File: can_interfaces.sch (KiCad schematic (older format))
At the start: 14 parts

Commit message: interface panel connector
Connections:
- net CAN1L: now reaches CONN?.4 (CANL), CONN?.4 (CANL), CONN?.4 (CANL), CONN?.4 (CANL), CONN?.4 (CANL), CONN?.4 (CANL), CONN?.4 (CANL), U?.6 (CANL)
- net CAN1H: now reaches CONN?.3 (CANH), CONN?.3 (CANH), CONN?.3 (CANH), CONN?.3 (CANH), CONN?.3 (CANH), CONN?.3 (CANH), CONN?.3 (CANH), U?.7 (CANH)
- net CAN2L: now reaches CONN?.4 (CANL), CONN?.4 (CANL), CONN?.4 (CANL), U?.6 (CANL)
- net CAN2H: now reaches CONN?.3 (CANH), CONN?.3 (CANH), CONN?.3 (CANH), U?.7 (CANH)
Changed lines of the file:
@@
 	1    0    0    -1
 $EndComp
+Text HLabel 4100 1000 0    60   BiDi ~ 0
+CAN1H
+Text HLabel 4100 1100 0    60   BiDi ~ 0
+CAN1L
+Text HLabel 9300 1000 0    60   BiDi ~ 0
+CAN2H
+Text HLabel 9300 1100 0    60   BiDi ~ 0
+CAN2L
 Wire Wire Line
 	2250 2100 2250 2150
@@
 	4300 6500 4400 6500
 Wire Wire Line
-	4300 1700 4300 6500
+	4300 1000 4300 6500
 Connection ~ 4300 1700
 Wire Wire Line
 	4200 6600 4400 6600
 Wire Wire Line
-	4200 1800 4200 6600
+	4200 1100 4200 6600
 Connection ~ 4200 1800
 Wire Wire Line
@@
 Connection ~ 4300 5700
 Wire Wire Line
-	9600 3300 9500 3300
+	9500 3300 9600 3300
 Wire Wire Line
-	9600 3400 9400 3400
+	9400 3400 9600 3400
 Wire Wire Line
 	9600 2600 9400 2600
@@
 Connection ~ 9500 2500
 Wire Wire Line
-	9600 1700 8900 1700
+	8900 1700 9600 1700
 Wire Wire Line
 	8900 1800 9600 1800
 Wire Wire Line
-	9400 3400 9400 1800
+	9400 1100 9400 3400
 Connection ~ 9400 1800
 Wire Wire Line
-	9500 3300 9500 1700
+	9500 1000 9500 3300
 Connection ~ 9500 1700
+Wire Wire Line
+	4100 1100 4200 1100
+Wire Wire Line
+	4300 1000 4100 1000
+Wire Wire Line
+	9300 1100 9400 1100
+Wire Wire Line
+	9300 1000 9500 1000
 $EndSCHEMATC

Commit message: gpio assignment, servos PWM chip
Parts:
- removed CONN?: CAN, MODULE, symbol CAN
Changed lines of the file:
@@
 $Descr A4 11693 8268
 encoding utf-8
-Sheet 2 2
+Sheet 2 3
 Title ""
 Date ""
@@
 	1    0    0    -1
 $EndComp
-$Comp
-L CAN CONN?
-U 1 1 5817684A
-P 9950 3250
-F 0 "CONN?" H 9950 3600 50  0000 C CNN
-F 1 "CAN" H 9950 2900 50  0000 C CNN
-F 2 "MODULE" H 10200 3250 50  0001 C CNN
-F 3 "DOCUMENTATION" H 10200 3250 50  0001 C CNN
-	1    9950 3250
-	1    0    0    -1
-$EndComp
-$Comp
-L GND #PWR?
-U 1 1 58176850
-P 9600 3200
-F 0 "#PWR?" H 9600 3200 30  0001 C CNN
-F 1 "GND" H 9600 3130 30  0001 C CNN
-F 2 "" H 9600 3200 60  0000 C CNN
-F 3 "" H 9600 3200 60  0000 C CNN
-	1    9600 3200
-	1    0    0    -1
-$EndComp
-$Comp
-L +5V #PWR?
-U 1 1 58176856
-P 9600 3100
-F 0 "#PWR?" H 9600 3190 20  0001 C CNN
-F 1 "+5V" H 9600 3190 30  0000 C CNN
-F 2 "" H 9600 3100 60  0000 C CNN
-F 3 "" H 9600 3100 60  0000 C CNN
-	1    9600 3100
-	1    0    0    -1
-$EndComp
 Text HLabel 4100 1000 0    60   BiDi ~ 0
 CAN1H
@@
 Connection ~ 4300 5700
 Wire Wire Line
-	9500 3300 9600 3300
-Wire Wire Line
-	9400 3400 9600 3400
-Wire Wire Line
-	9600 2600 9400 2600
-Connection ~ 9400 2600
-Wire Wire Line
-	9600 2500 9500 2500
-Connection ~ 9500 2500
+	9400 2600 9600 2600
+Wire Wire Line
+	9500 2500 9600 2500
 Wire Wire Line
 	8900 1700 9600 1700
@@
 	8900 1800 9600 1800
 Wire Wire Line
-	9400 1100 9400 3400
+	9400 1100 9400 2600
 Connection ~ 9400 1800
 Wire Wire Line
-	9500 1000 9500 3300
+	9500 1000 9500 2500
 Connection ~ 9500 1700
 Wire Wire Line

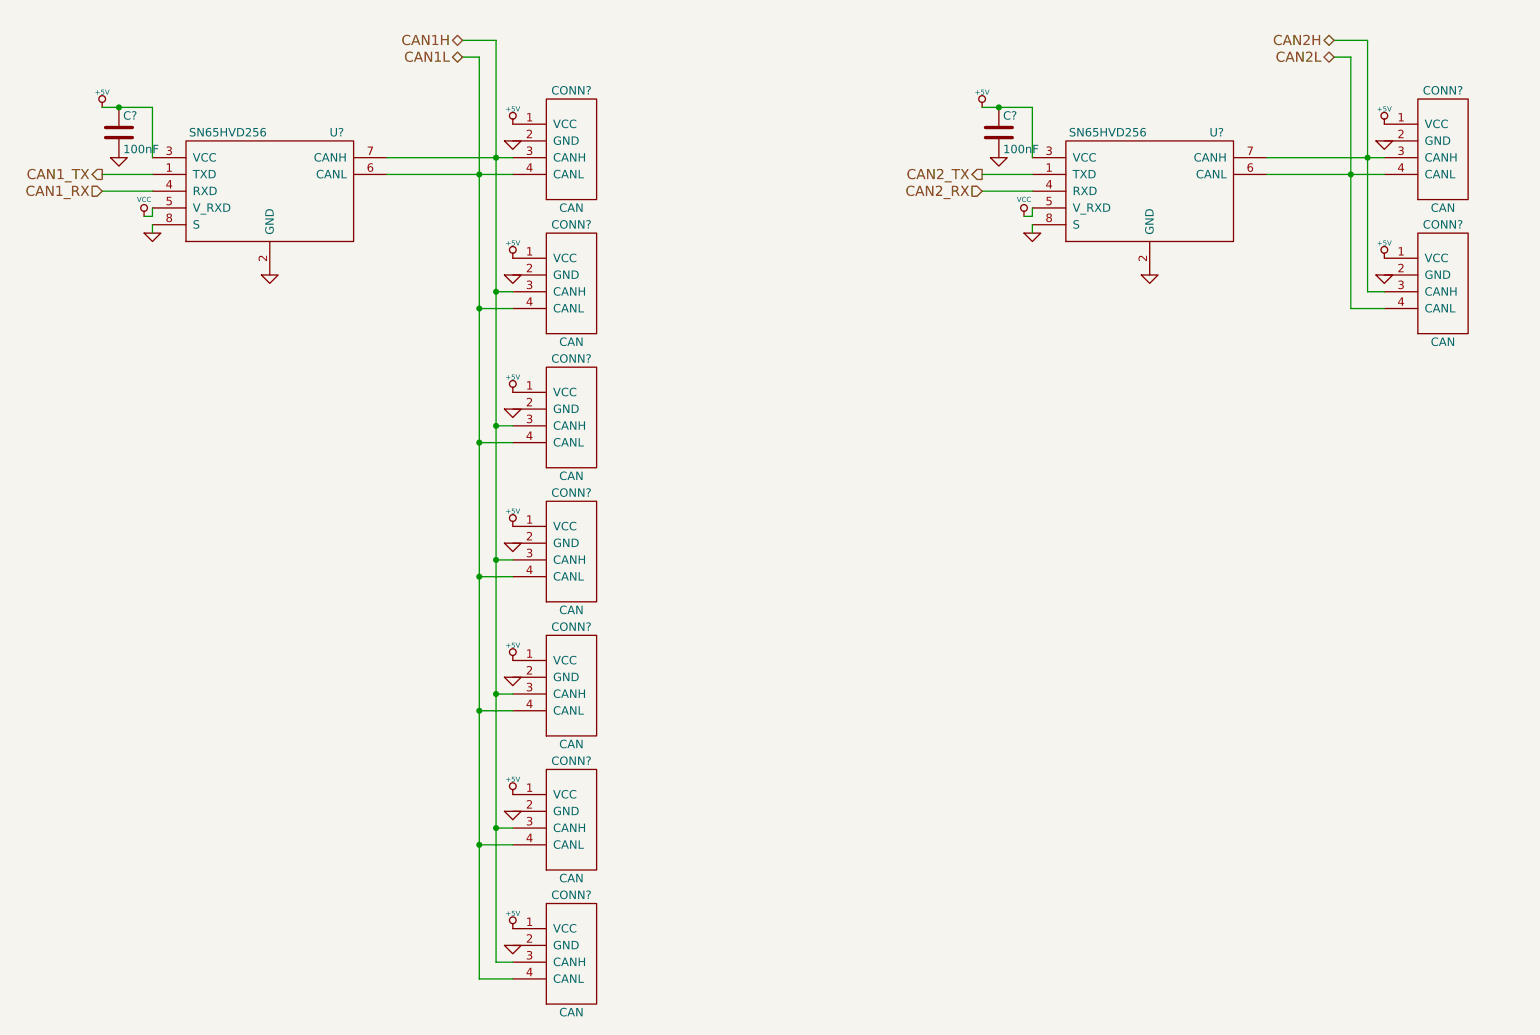
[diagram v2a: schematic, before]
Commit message: pin assignment, separate CAN_5V
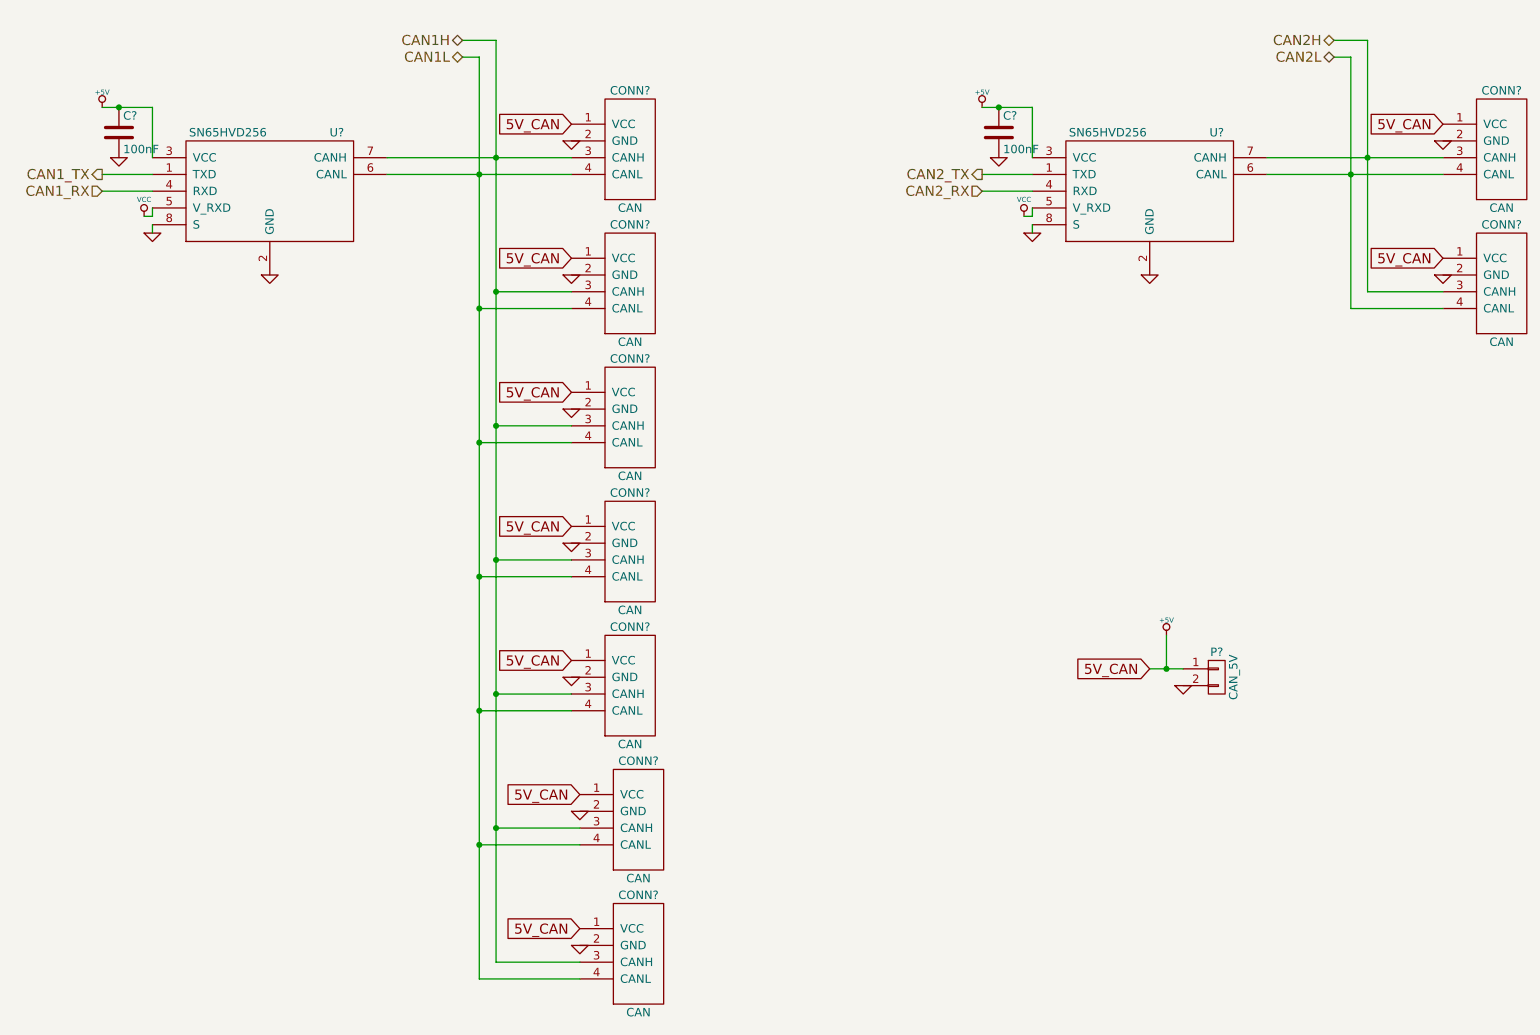
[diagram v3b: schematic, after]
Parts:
- added P?: CAN_5V, symbol CONN_01X02
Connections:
- net +5V: now also P?.1 (P1)
- net GND: now also P?.2 (P2)
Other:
- moved on the sheet: CONN?

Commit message: footprint assignment
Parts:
- removed P?: CAN_5V, symbol CONN_01X02
- C3, C4: renamed from C?; footprint (none) -> Capacitors_SMD:C_0603
- CONN10, CONN11, CONN12, CONN13, CONN14, CONN6, CONN7, CONN8, CONN9: renamed from CONN?; footprint MODULE -> _connectors:_Molex-PicoBlade-SMD-4
- U2, U3: renamed from U?; footprint MODULE -> _std:_SO-8
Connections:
- net +5V: no longer CONN10.1 (VCC), CONN11.1 (VCC), CONN12.1 (VCC), CONN13.1 (VCC), CONN14.1 (VCC), CONN6.1 (VCC), CONN7.1 (VCC), CONN8.1 (VCC), CONN9.1 (VCC)
- net VCC renamed +3.3V
- new net 5V_CAN1: CONN10.1 (VCC), CONN11.1 (VCC), CONN12.1 (VCC), CONN6.1 (VCC), CONN7.1 (VCC), CONN8.1 (VCC), CONN9.1 (VCC)
- new net 5V_CAN2: CONN13.1 (VCC), CONN14.1 (VCC)
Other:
- moved on the sheet: CONN10, CONN11, CONN12, CONN13, CONN14, CONN6, CONN7, CONN8, CONN9

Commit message: place parts in PCB
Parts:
- C3, C4: footprint Capacitors_SMD:C_0603 -> Capacitors_SMD:C_0805
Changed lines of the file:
@@
 $EndComp
 $Comp
-L GND #PWR040
+L GND #PWR041
 U 1 1 581746BE
 P 2250 2150
-F 0 "#PWR040" H 2250 2150 30  0001 C CNN
+F 0 "#PWR041" H 2250 2150 30  0001 C CNN
 F 1 "GND" H 2250 2080 30  0001 C CNN
 F 2 "" H 2250 2150 60  0000 C CNN
@@
 $EndComp
 $Comp
-L GND #PWR041
+L GND #PWR042
 U 1 1 581746D7
 P 2950 2400
-F 0 "#PWR041" H 2950 2400 30  0001 C CNN
+F 0 "#PWR042" H 2950 2400 30  0001 C CNN
 F 1 "GND" H 2950 2330 30  0001 C CNN
 F 2 "" H 2950 2400 60  0000 C CNN
@@
 F 0 "C3" H 2075 1650 50  0000 L CNN
 F 1 "100nF" H 2075 1450 50  0000 L CNN
-F 2 "Capacitors_SMD:C_0603" H 2088 1400 50  0001 C CNN
+F 2 "Capacitors_SMD:C_0805" H 2088 1400 50  0001 C CNN
 F 3 "" H 2050 1550 50  0000 C CNN
 	1    2050 1550
@@
 $EndComp
 $Comp
-L GND #PWR042
+L GND #PWR043
 U 1 1 58174920
 P 2050 1700
-F 0 "#PWR042" H 2050 1700 30  0001 C CNN
+F 0 "#PWR043" H 2050 1700 30  0001 C CNN
 F 1 "GND" H 2050 1630 30  0001 C CNN
 F 2 "" H 2050 1700 60  0000 C CNN
@@
 $EndComp
 $Comp
-L GND #PWR043
+L GND #PWR044
 U 1 1 581752A3
 P 7500 2150
-F 0 "#PWR043" H 7500 2150 30  0001 C CNN
+F 0 "#PWR044" H 7500 2150 30  0001 C CNN
 F 1 "GND" H 7500 2080 30  0001 C CNN
 F 2 "" H 7500 2150 60  0000 C CNN
@@
 $EndComp
 $Comp
-L GND #PWR044
+L GND #PWR045
 U 1 1 581752BE
 P 8200 2400
-F 0 "#PWR044" H 8200 2400 30  0001 C CNN
+F 0 "#PWR045" H 8200 2400 30  0001 C CNN
 F 1 "GND" H 8200 2330 30  0001 C CNN
 F 2 "" H 8200 2400 60  0000 C CNN
@@
 F 0 "C4" H 7325 1650 50  0000 L CNN
 F 1 "100nF" H 7325 1450 50  0000 L CNN
-F 2 "Capacitors_SMD:C_0603" H 7338 1400 50  0001 C CNN
+F 2 "Capacitors_SMD:C_0805" H 7338 1400 50  0001 C CNN
 F 3 "" H 7300 1550 50  0000 C CNN
 	1    7300 1550
@@
 $EndComp
 $Comp
-L +5V #PWR045
+L +5V #PWR046
 U 1 1 58175498
 P 7200 1400
-F 0 "#PWR045" H 7200 1490 20  0001 C CNN
+F 0 "#PWR046" H 7200 1490 20  0001 C CNN
 F 1 "+5V" H 7200 1490 30  0000 C CNN
 F 2 "" H 7200 1400 60  0000 C CNN
@@
 $EndComp
 $Comp
-L GND #PWR046
+L GND #PWR047
 U 1 1 581754CD
 P 7300 1700
-F 0 "#PWR046" H 7300 1700 30  0001 C CNN
+F 0 "#PWR047" H 7300 1700 30  0001 C CNN
 F 1 "GND" H 7300 1630 30  0001 C CNN
 F 2 "" H 7300 1700 60  0000 C CNN
@@
 $EndComp
 $Comp
-L GND #PWR047
+L GND #PWR048
 U 1 1 58176079
 P 4550 1600
-F 0 "#PWR047" H 4550 1600 30  0001 C CNN
+F 0 "#PWR048" H 4550 1600 30  0001 C CNN
 F 1 "GND" H 4550 1530 30  0001 C CNN
 F 2 "" H 4550 1600 60  0000 C CNN
@@
 $EndComp
 $Comp
-L GND #PWR048
+L GND #PWR049
 U 1 1 5817609F
 P 4550 2400
-F 0 "#PWR048" H 4550 2400 30  0001 C CNN
+F 0 "#PWR049" H 4550 2400 30  0001 C CNN
 F 1 "GND" H 4550 2330 30  0001 C CNN
 F 2 "" H 4550 2400 60  0000 C CNN
@@
 $EndComp
 $Comp
-L GND #PWR049
+L GND #PWR050
 U 1 1 581760FF
 P 4550 3200
-F 0 "#PWR049" H 4550 3200 30  0001 C CNN
+F 0 "#PWR050" H 4550 3200 30  0001 C CNN
 F 1 "GND" H 4550 3130 30  0001 C CNN
 F 2 "" H 4550 3200 60  0000 C CNN
@@
 $EndComp
 $Comp
-L GND #PWR050
+L GND #PWR051
 U 1 1 58176161
 P 4550 4000
-F 0 "#PWR050" H 4550 4000 30  0001 C CNN
+F 0 "#PWR051" H 4550 4000 30  0001 C CNN
 F 1 "GND" H 4550 3930 30  0001 C CNN
 F 2 "" H 4550 4000 60  0000 C CNN
@@
 $EndComp
 $Comp
-L GND #PWR051
+L GND #PWR052
 U 1 1 58176173
 P 4550 4800
-F 0 "#PWR051" H 4550 4800 30  0001 C CNN
+F 0 "#PWR052" H 4550 4800 30  0001 C CNN
 F 1 "GND" H 4550 4730 30  0001 C CNN
 F 2 "" H 4550 4800 60  0000 C CNN
@@
 $EndComp
 $Comp
-L GND #PWR052
+L GND #PWR053
 U 1 1 581761CE
 P 4550 5600
-F 0 "#PWR052" H 4550 5600 30  0001 C CNN
+F 0 "#PWR053" H 4550 5600 30  0001 C CNN
 F 1 "GND" H 4550 5530 30  0001 C CNN
 F 2 "" H 4550 5600 60  0000 C CNN
@@
 $EndComp
 $Comp
-L GND #PWR053
+L GND #PWR054
 U 1 1 581761E0
 P 4550 6400
-F 0 "#PWR053" H 4550 6400 30  0001 C CNN
+F 0 "#PWR054" H 4550 6400 30  0001 C CNN
 F 1 "GND" H 4550 6330 30  0001 C CNN
 F 2 "" H 4550 6400 60  0000 C CNN
@@
 $EndComp
 $Comp
-L GND #PWR054
+L GND #PWR055
 U 1 1 5817682C
 P 9750 1600
-F 0 "#PWR054" H 9750 1600 30  0001 C CNN
+F 0 "#PWR055" H 9750 1600 30  0001 C CNN
 F 1 "GND" H 9750 1530 30  0001 C CNN
 F 2 "" H 9750 1600 60  0000 C CNN
@@
 $EndComp
 $Comp
-L GND #PWR055
+L GND #PWR056
 U 1 1 5817683E
 P 9750 2400
-F 0 "#PWR055" H 9750 2400 30  0001 C CNN
+F 0 "#PWR056" H 9750 2400 30  0001 C CNN
 F 1 "GND" H 9750 2330 30  0001 C CNN
 F 2 "" H 9750 2400 60  0000 C CNN
@@
 Connection ~ 9600 1500
 $Comp
-L +5V #PWR056
+L +5V #PWR057
 U 1 1 58174882
 P 1950 1400
-F 0 "#PWR056" H 1950 1490 20  0001 C CNN
+F 0 "#PWR057" H 1950 1490 20  0001 C CNN
 F 1 "+5V" H 1950 1490 30  0000 C CNN
 F 2 "" H 1950 1400 60  0000 C CNN
@@
 $EndComp
 $Comp
-L +3.3V #PWR057
+L +3.3V #PWR058
 U 1 1 58BBAC69
 P 2200 2050
-F 0 "#PWR057" H 2200 2010 30  0001 C CNN
+F 0 "#PWR058" H 2200 2010 30  0001 C CNN
 F 1 "+3.3V" H 2200 2160 30  0000 C CNN
 F 2 "" H 2200 2050 60  0001 C CNN
@@
 $EndComp
 $Comp
-L +3.3V #PWR058
+L +3.3V #PWR059
 U 1 1 58BBACF3
 P 7450 2050
-F 0 "#PWR058" H 7450 2010 30  0001 C CNN
+F 0 "#PWR059" H 7450 2010 30  0001 C CNN
 F 1 "+3.3V" H 7450 2160 30  0000 C CNN
 F 2 "" H 7450 2050 60  0001 C CNN

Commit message: PCB routing
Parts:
- U2, U3: footprint _std:_SO-8 -> Housings_SOIC:SOIC-8_3.9x4.9mm_Pitch1.27mm
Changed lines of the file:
@@
 F 0 "U2" H 3350 2250 50  0000 C CNN
 F 1 "SN65HVD256" H 2700 2250 50  0000 C CNN
-F 2 "_std:_SO-8" H 2950 1900 50  0001 C CNN
+F 2 "Housings_SOIC:SOIC-8_3.9x4.9mm_Pitch1.27mm" H 2950 1900 50  0001 C CNN
 F 3 "CAN Transceiver" H 2950 2000 50  0001 C CNN
 	1    2950 1900
@@
 F 0 "U3" H 8600 2250 50  0000 C CNN
 F 1 "SN65HVD256" H 7950 2250 50  0000 C CNN
-F 2 "_std:_SO-8" H 8200 1900 50  0001 C CNN
+F 2 "Housings_SOIC:SOIC-8_3.9x4.9mm_Pitch1.27mm" H 8200 1900 50  0001 C CNN
 F 3 "CAN Transceiver" H 8200 2000 50  0001 C CNN
 	1    8200 1900
